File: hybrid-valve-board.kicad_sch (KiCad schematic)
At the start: 46 parts, among them J1 XV Supply, J10 ARM, J2 MCU Supply, J3 XV In, J4 XV In, J5 XV In, J6 Continuity, J7 XV Out, J8 XV Out, J9 XV Out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

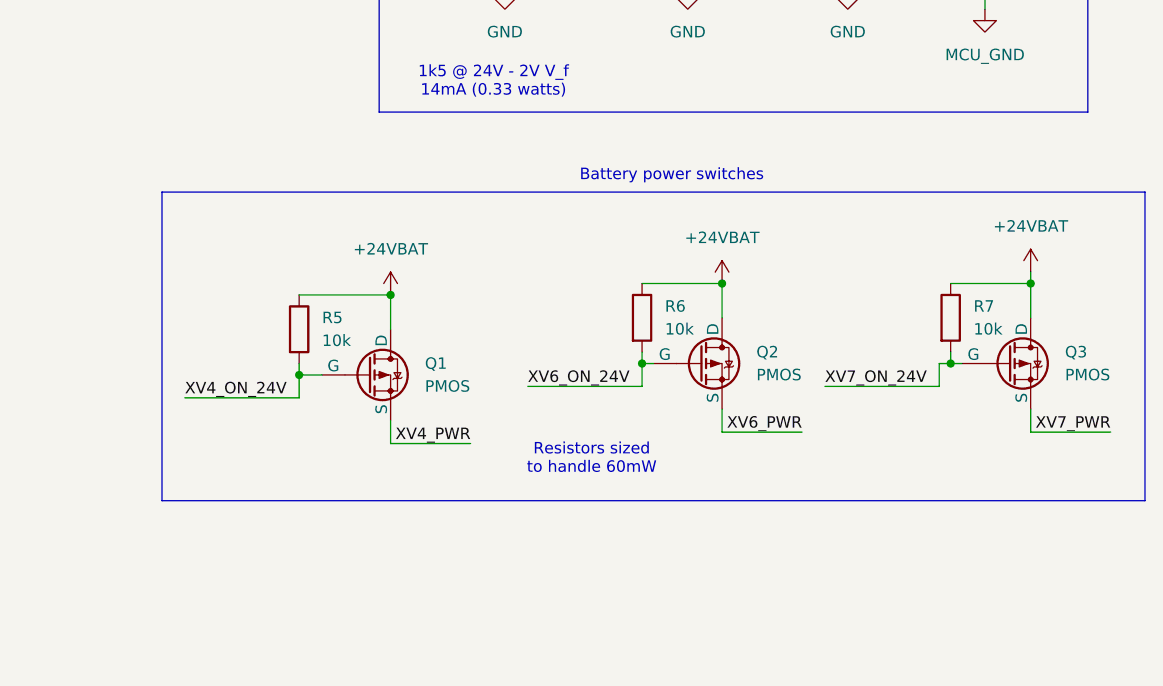
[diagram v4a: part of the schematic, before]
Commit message: Revision B, with correct connections for the PMOS switches :/
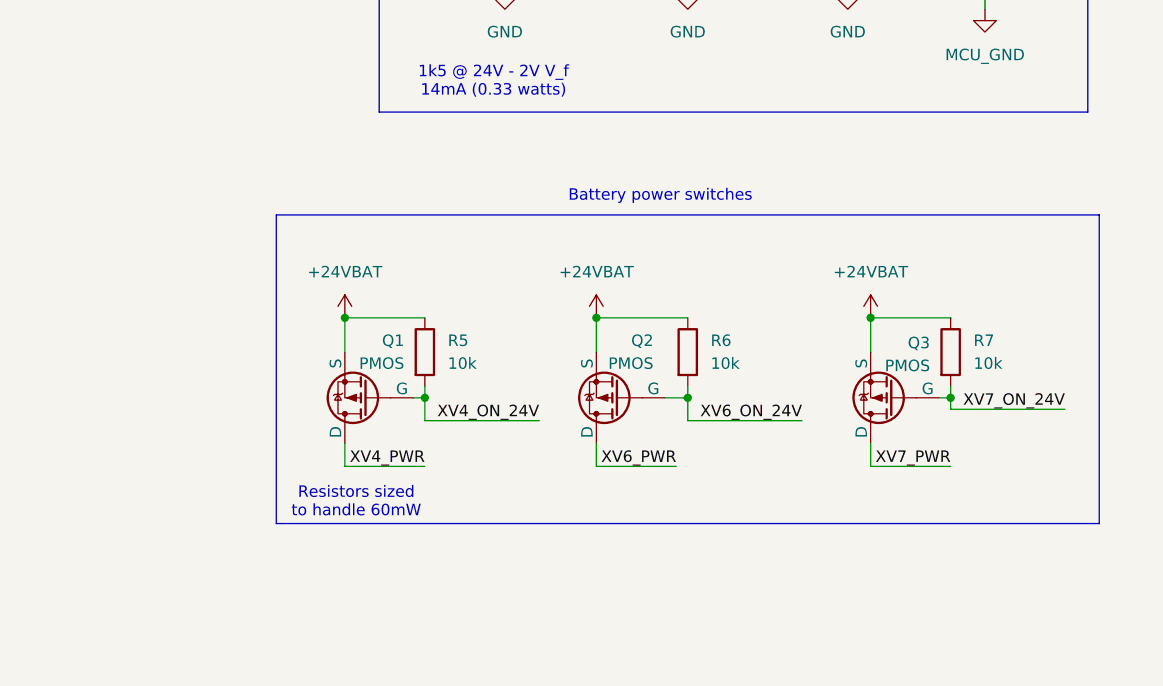
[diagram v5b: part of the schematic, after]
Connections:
- net +24VBAT: now also Q1.3 (S), Q2.3 (S), Q3.3 (S); no longer Q1.2 (D), Q2.2 (D), Q3.2 (D)
- net XV4_PWR: now also Q1.2 (D); no longer Q1.3 (S)
- net XV6_PWR: now also Q2.2 (D); no longer Q2.3 (S)
- net XV7_PWR: now also Q3.2 (D); no longer Q3.3 (S)
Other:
- moved on the sheet: R6, R7

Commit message: Move LED indicators to power line to avoid interfering with gate signal
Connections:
- net XV4_ON_24V: no longer D7.2 (A)
- net XV4_PWR: now also D7.2 (A)
- net XV6_ON_24V: no longer D8.2 (A)
- net XV6_PWR: now also D8.2 (A)
- net XV7_ON_24V: no longer D9.2 (A)
- net XV7_PWR: now also D9.2 (A)
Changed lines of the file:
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@@
 		)
 	)
-	(label "XV4_ON_24V"
+	(label "XV4_PWR"
 		(at 210.82 67.31 180)
 		(fields_autoplaced yes)
@@
 		)
 	)
-	(label "XV6_ON_24V"
+	(label "XV6_PWR"
 		(at 231.14 67.31 180)
 		(fields_autoplaced yes)
@@
 		)
 	)
-	(label "XV7_ON_24V"
+	(label "XV7_PWR"
 		(at 248.92 67.31 180)
 		(fields_autoplaced yes)

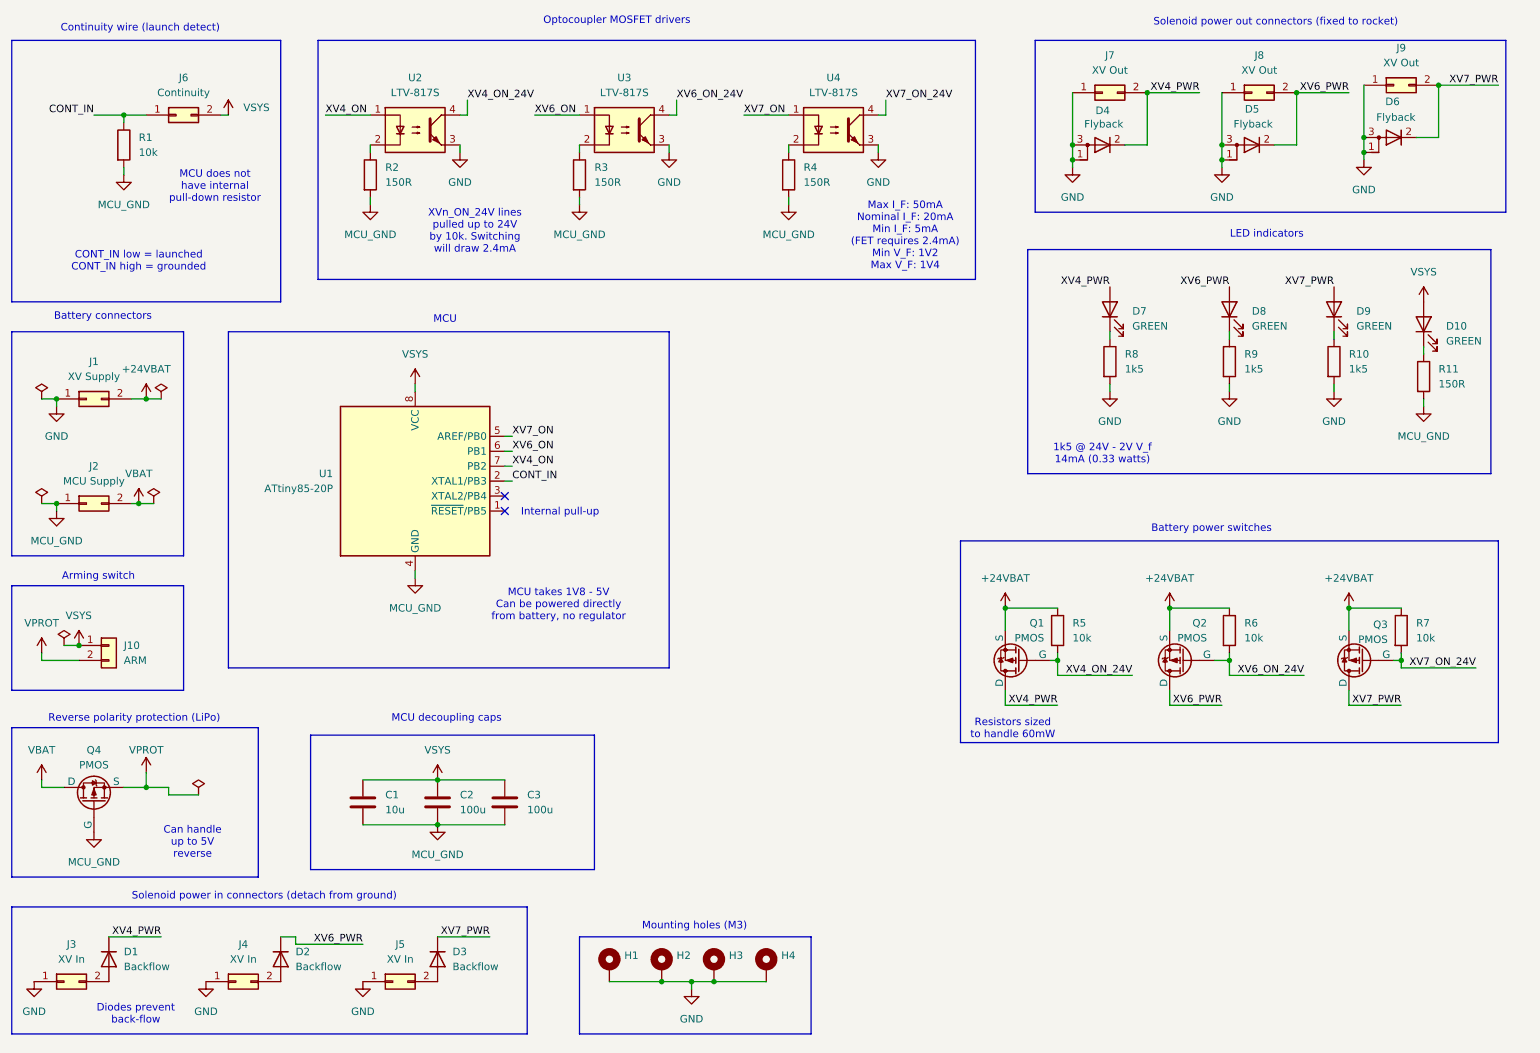
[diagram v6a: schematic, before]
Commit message: Use NMOS to flip opto-coupler
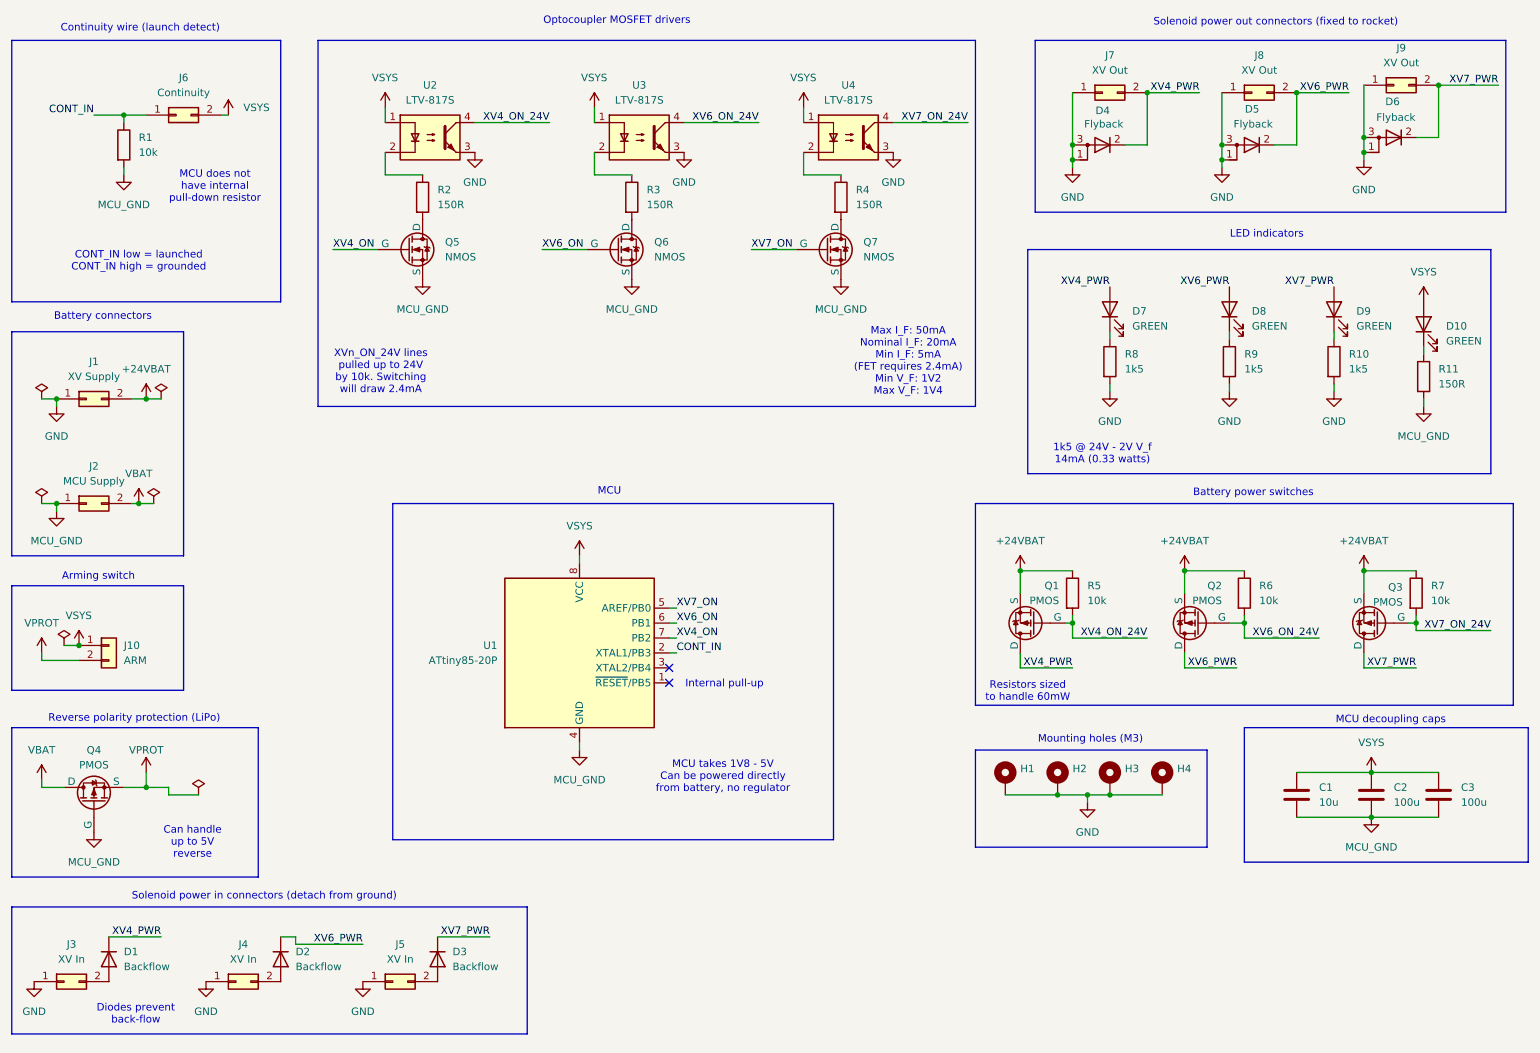
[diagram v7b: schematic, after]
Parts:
- added Q5, Q6, Q7: NMOS, Package_TO_SOT_SMD:SOT-23-3, symbol Simulation_SPICE:NMOS
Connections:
- net MCU_GND: now also Q5.2 (S), Q6.2 (S), Q7.2 (S); no longer R2.2, R3.2, R4.2
- net VSYS: now also U2.1, U3.1, U4.1
- net XV4_ON: now also Q5.1 (G); no longer U2.1
- net XV6_ON: now also Q6.1 (G); no longer U3.1
- net XV7_ON: now also Q7.1 (G); no longer U4.1
- new net: Q5.3 (D), R2.2
- new net: Q6.3 (D), R3.2
- new net: Q7.3 (D), R4.2
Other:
- moved on the sheet: C1, C2, C3, H1, H2, H3, H4, Q1, Q2, Q3, R3, R4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

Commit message: Add pull-down resistor on NMOS gate
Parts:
- added R12, R13, R14: 10k, Resistor_SMD:R_0805_2012Metric_Pad1.20x1.40mm_HandSolder, symbol Device:R
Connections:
- net MCU_GND: now also R12.2, R13.2, R14.2
- net XV4_ON: now also R12.1
- net XV6_ON: now also R13.1
- net XV7_ON: now also R14.1
